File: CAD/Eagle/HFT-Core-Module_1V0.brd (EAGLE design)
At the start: 96.5 x 96.5 mm, 341 parts, among them Q0521 ABS07-32.768KHZ, Q0911 ABM3B-16MHZ-10-R50-1-U, T0801 MMBT2222, T0802 MMBT2222, T0803 MMBT2222, U0111 STM32L4Z_144PIN_SMPS, U0431 PAM2305AAB120, U0601 LM4120IM5-3.0, U0611 MAX5217, U0631 CFPT-141-20MHZ, U0641 OPA354, U0701 Si5338, U0801 NHD-C0220BIZ_2X20CHARS, U0901 AX5243, U1001 AX5243, U1101 MCP3911A0-E-SS, U1111 MAX5136AGTG+, U1121 OPA354, U1131 OPA354, U1141 OPA354, U1601 SOLARPANEL_3V3_5MA1_25MM_X_20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, U1602 SPV1040T, U1701 TS5A23166, U1801 PAM2305AAB330, U1901 TS5A23166, U2001 TS5A23166, U2101 TS5A23166, X0861 TTE_EN11-HSM, X1401 SMA_SMT_AMPHENOL-901-143, X1411 SMA_SMT_AMPHENOL-901-143, X1501 CUI SJ1-3535NS, X1511 CUI SJ1-3535NS, X511 2X20/90_1MM27_HARWIN_M50-3202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, X512 2X20/90_1MM27_HARWIN_M50-3202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, X521 2X20/90_1MM27_HARWIN_M50-3202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, X522 2X20/90_1MM27_HARWIN_M50-3202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, X531 2X20/90_1MM27_HARWIN_M50-3202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, X532 2X20/90_1MM27_HARWIN_M50-3202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

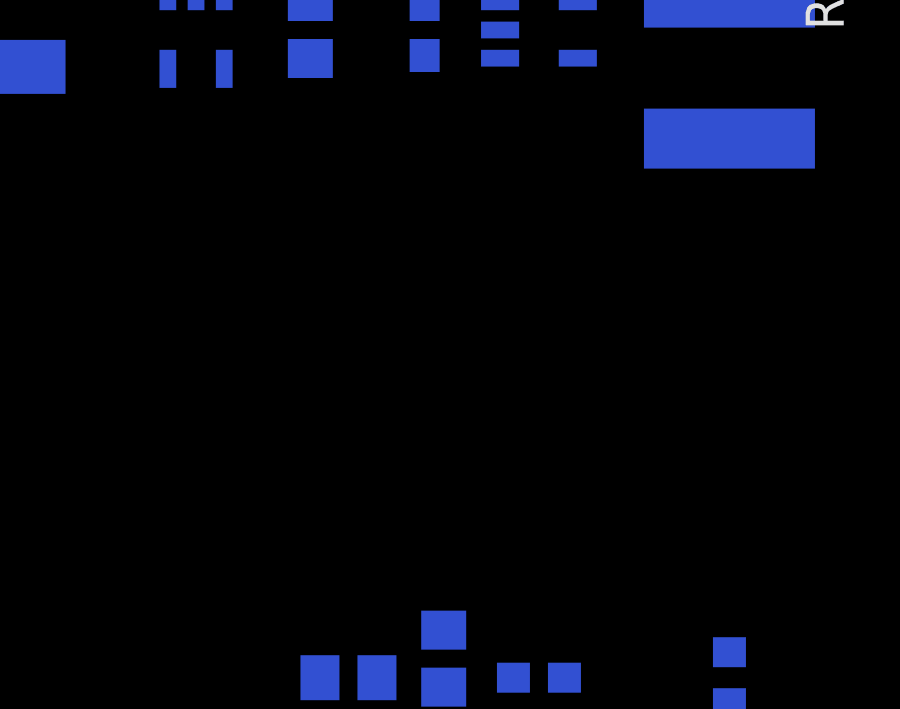
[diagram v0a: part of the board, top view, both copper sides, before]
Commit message: HW_1V0 - MPU-9250 added and placed
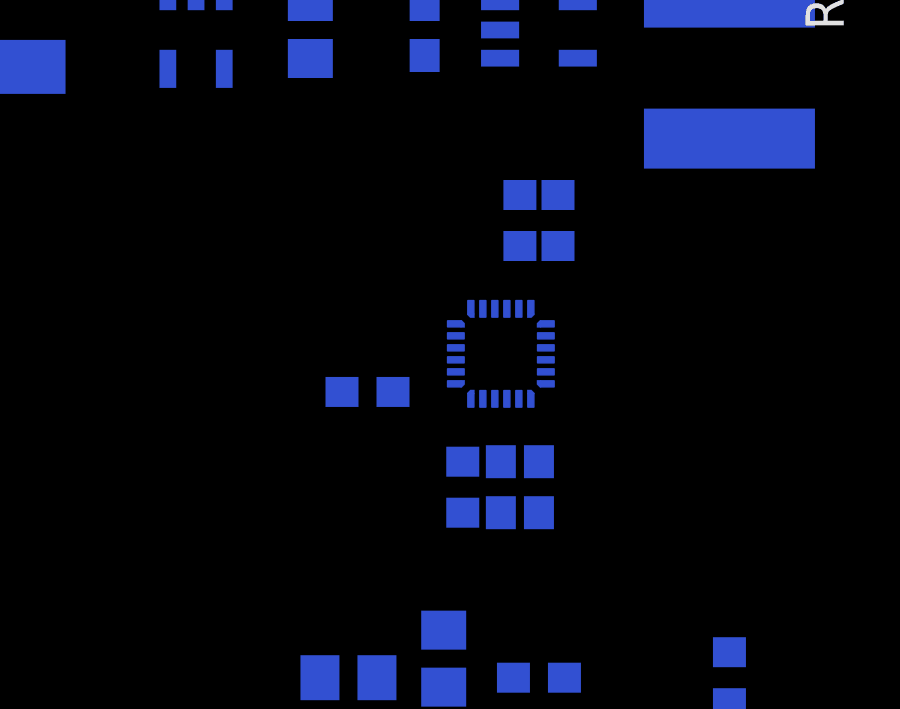
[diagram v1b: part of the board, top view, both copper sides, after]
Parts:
- added C2301, C2303: 100nF, rcl:C0603
- added C2302: 10nF, rcl:C0603
- added R2301: 68R, rcl:R0603
- added R2311, R2312: 3.9kR, rcl:R0603
- added U2301: MPU-9250, df4iah_sensors:QFN24-3X3
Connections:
- new net I2C2_INT: R2301.2
- new net MPU_INT: R2301.1, U2301.12
- new net MPU_REGOUT: C2303.1, U2301.10
- net +3V3: now also C2301.1, C2302.1, R2311.2, R2312.2, U2301.1, U2301.13, U2301.22, U2301.8
- net GND: now also C2301.2, C2302.2, C2303.2, U2301.11, U2301.18, U2301.20, U2301.9
- net MCU_I2C4_SCL: now also R2312.1, U2301.23
- net MCU_I2C4_SDA: now also R2311.1, U2301.24
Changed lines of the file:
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@@
 <element name="R0804" library="rcl" package="R0603" value="2.2kR" x="59.055" y="47.625" rot="R90"/>
 <element name="R0801" library="rcl" package="R0603" value="1.8kR" x="80.645" y="65.405" rot="MR0"/>
+<element name="U2301" library="df4iah_sensors" package="QFN24-3X3" value="MPU-9250" x="48.26" y="23.495" rot="MR0"/>
+<element name="C2301" library="rcl" package="C0603" value="100nF" x="49.53" y="19.05" rot="MR270"/>
+<element name="C2303" library="rcl" package="C0603" value="100nF" x="48.26" y="19.05" rot="MR270"/>
+<element name="R2301" library="rcl" package="R0603" value="68R" x="46.99" y="19.05" rot="MR270"/>
+<element name="C2302" library="rcl" package="C0603" value="10nF" x="43.815" y="22.225" rot="MR0"/>
+<element name="R2311" library="rcl" package="R0603" value="3.9kR" x="50.165" y="27.94" rot="MR90"/>
+<element name="R2312" library="rcl" package="R0603" value="3.9kR" x="48.895" y="27.94" rot="MR90"/>
 </elements>
 <signals>
@@
 <contactref element="R0802" pad="1"/>
 <contactref element="R0805" pad="1"/>
+<contactref element="U2301" pad="9"/>
+<contactref element="C2301" pad="2"/>
+<contactref element="U2301" pad="20"/>
+<contactref element="U2301" pad="18"/>
+<contactref element="U2301" pad="11"/>
+<contactref element="C2303" pad="2"/>
+<contactref element="C2302" pad="2"/>
 <wire x1="93.7025" y1="87.6" x2="91.44" y2="91.44" width="0" layer="19" extent="1-1"/>
 <wire x1="93.56" y1="85.725" x2="93.7025" y2="87.6" width="0" layer="19" extent="16-16"/>
@@
 <wire x1="63.285" y1="11.43" x2="63.285" y2="10.16" width="0" layer="19" extent="16-16"/>
 <wire x1="46.355" y1="14.285" x2="50.38" y2="12.7" width="0" layer="19" extent="16-16"/>
+<wire x1="48.26" y1="18.2" x2="46.355" y2="14.285" width="0" layer="19" extent="16-16"/>
+<wire x1="49.53" y1="18.2" x2="48.26" y2="18.2" width="0" layer="19" extent="16-16"/>
+<wire x1="48.46" y1="21.995" x2="48.26" y2="18.2" width="0" layer="19" extent="16-16"/>
+<wire x1="47.66" y1="21.995" x2="48.46" y2="21.995" width="0" layer="19" extent="16-16"/>
+<wire x1="46.7075" y1="24.495" x2="47.66" y2="21.995" width="0" layer="19" extent="16-16"/>
+<wire x1="47.66" y1="24.995" x2="46.7075" y2="24.495" width="0" layer="19" extent="16-16"/>
+<wire x1="42.965" y1="22.225" x2="46.7075" y2="24.495" width="0" layer="19" extent="16-16"/>
 <wire x1="62.23" y1="2.54" x2="62.23" y2="7.62" width="0" layer="19" extent="1-1"/>
 <wire x1="58.42" y1="2.54" x2="62.23" y2="2.54" width="0" layer="19" extent="1-1"/>
@@
 <contactref element="U0111" pad="106"/>
 <contactref element="U0801" pad="12"/>
+<contactref element="U2301" pad="8"/>
+<contactref element="U2301" pad="1"/>
+<contactref element="U2301" pad="13"/>
+<contactref element="C2301" pad="1"/>
+<contactref element="U2301" pad="22"/>
+<contactref element="C2302" pad="1"/>
+<contactref element="R2311" pad="2"/>
+<contactref element="R2312" pad="2"/>
 <wire x1="73.66" y1="88.9" x2="85.09" y2="90.17" width="0" layer="19" extent="1-1"/>
 <wire x1="73.66" y1="93.98" x2="73.66" y2="88.9" width="0" layer="19" extent="1-1"/>
@@
 <wire x1="48.2346" y1="35.2298" x2="45.72" y2="35.14" width="0" layer="19" extent="16-16"/>
 <wire x1="48.2346" y1="33.3502" x2="48.2346" y2="35.2298" width="0" layer="19" extent="16-16"/>
+<wire x1="48.895" y1="28.79" x2="48.2346" y2="33.3502" width="0" layer="19" extent="16-16"/>
+<wire x1="50.165" y1="28.79" x2="48.895" y2="28.79" width="0" layer="19" extent="16-16"/>
+<wire x1="48.46" y1="24.995" x2="48.895" y2="28.79" width="0" layer="19" extent="16-16"/>
+<wire x1="49.8125" y1="24.495" x2="48.46" y2="24.995" width="0" layer="19" extent="16-16"/>
+<wire x1="48.86" y1="21.995" x2="49.8125" y2="24.495" width="0" layer="19" extent="16-16"/>
+<wire x1="49.53" y1="19.9" x2="48.86" y2="21.995" width="0" layer="19" extent="16-16"/>
+<wire x1="46.7075" y1="22.495" x2="48.86" y2="21.995" width="0" layer="19" extent="16-16"/>
+<wire x1="44.665" y1="22.225" x2="46.7075" y2="22.495" width="0" layer="19" extent="16-16"/>
+<wire x1="48.68" y1="12.7" x2="49.53" y2="19.9" width="0" layer="19" extent="16-16"/>
+<wire x1="48.276" y1="10.13" x2="48.68" y2="12.7" width="0" layer="19" extent="16-16"/>
 <wire x1="59.335" y1="37.985" x2="48.2346" y2="35.2298" width="0" layer="19" extent="16-16"/>
 <wire x1="60.96" y1="37.885" x2="59.335" y2="37.985" width="0" layer="19" extent="16-16"/>
@@
 <wire x1="73.66" y1="7.62" x2="68.85" y2="16.455" width="0" layer="19" extent="16-16"/>
 <wire x1="73.66" y1="2.54" x2="73.66" y2="7.62" width="0" layer="19" extent="1-1"/>
-<wire x1="48.68" y1="12.7" x2="68.16" y2="17.145" width="0" layer="19" extent="16-16"/>
-<wire x1="48.276" y1="10.13" x2="48.68" y2="12.7" width="0" layer="19" extent="16-16"/>
 <wire x1="22.86" y1="7.62" x2="48.276" y2="10.13" width="0" layer="19" extent="1-1"/>
 <wire x1="22.86" y1="2.54" x2="22.86" y2="7.62" width="0" layer="19" extent="1-1"/>
@@
 <contactref element="U0701" pad="12"/>
 <contactref element="R0231" pad="2"/>
+<contactref element="U2301" pad="23"/>
+<contactref element="R2312" pad="1"/>
 <wire x1="41.03" y1="83.495" x2="70.53" y2="84.435" width="0" layer="19" extent="1-1"/>
 <wire x1="66.04" y1="46.775" x2="70.53" y2="84.435" width="0" layer="19" extent="1-1"/>
-<wire x1="54.276" y1="10.13" x2="66.04" y2="46.775" width="0" layer="19" extent="1-1"/>
+<wire x1="48.895" y1="27.09" x2="66.04" y2="46.775" width="0" layer="19" extent="1-16"/>
+<wire x1="48.86" y1="24.995" x2="48.895" y2="27.09" width="0" layer="19" extent="16-16"/>
+<wire x1="54.276" y1="10.13" x2="48.86" y2="24.995" width="0" layer="19" extent="16-16"/>
 </signal>
 <signal name="MCU_I2C4_SDA">
@@
 <contactref element="U0701" pad="19"/>
 <contactref element="R0232" pad="2"/>
+<contactref element="U2301" pad="24"/>
+<contactref element="R2311" pad="1"/>
 <wire x1="41.03" y1="82.845" x2="66.63" y2="84.435" width="0" layer="19" extent="1-1"/>
 <wire x1="81.495" y1="58.42" x2="66.63" y2="84.435" width="0" layer="19" extent="1-1"/>
-<wire x1="52.276" y1="10.13" x2="81.495" y2="58.42" width="0" layer="19" extent="1-1"/>
+<wire x1="50.165" y1="27.09" x2="81.495" y2="58.42" width="0" layer="19" extent="1-16"/>
+<wire x1="49.26" y1="25.0475" x2="50.165" y2="27.09" width="0" layer="19" extent="16-16"/>
+<wire x1="52.276" y1="10.13" x2="49.26" y2="25.0475" width="0" layer="19" extent="16-16"/>
 </signal>
 <signal name="MCU_I2C2_SCL">
@@
 <wire x1="10.726" y1="28.18" x2="16.045" y2="22.86" width="0" layer="19" extent="16-16"/>
 </signal>
+<signal name="MPU_REGOUT">
+<contactref element="U2301" pad="10"/>
+<contactref element="C2303" pad="1"/>
+<wire x1="48.26" y1="19.9" x2="48.06" y2="21.995" width="0" layer="19" extent="16-16"/>
+</signal>
+<signal name="I2C2_INT">
+<contactref element="R2301" pad="2"/>
+</signal>
+<signal name="MPU_INT">
+<contactref element="U2301" pad="12"/>
+<contactref element="R2301" pad="1"/>
+<wire x1="46.99" y1="19.9" x2="47.26" y2="21.9425" width="0" layer="19" extent="16-16"/>
+</signal>
 </signals>

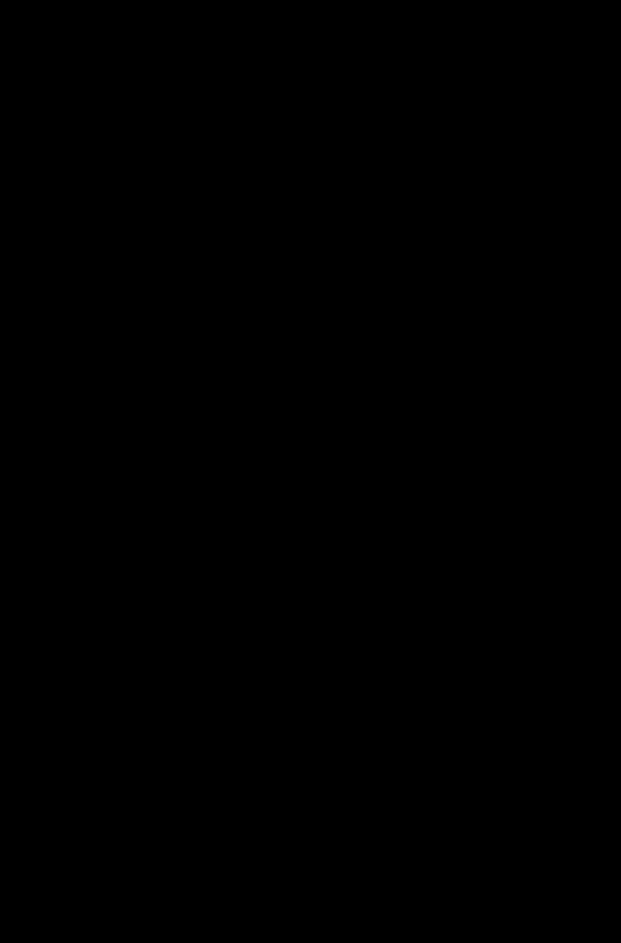
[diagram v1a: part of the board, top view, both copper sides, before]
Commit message: HW_1V0 - more I2C sensors added
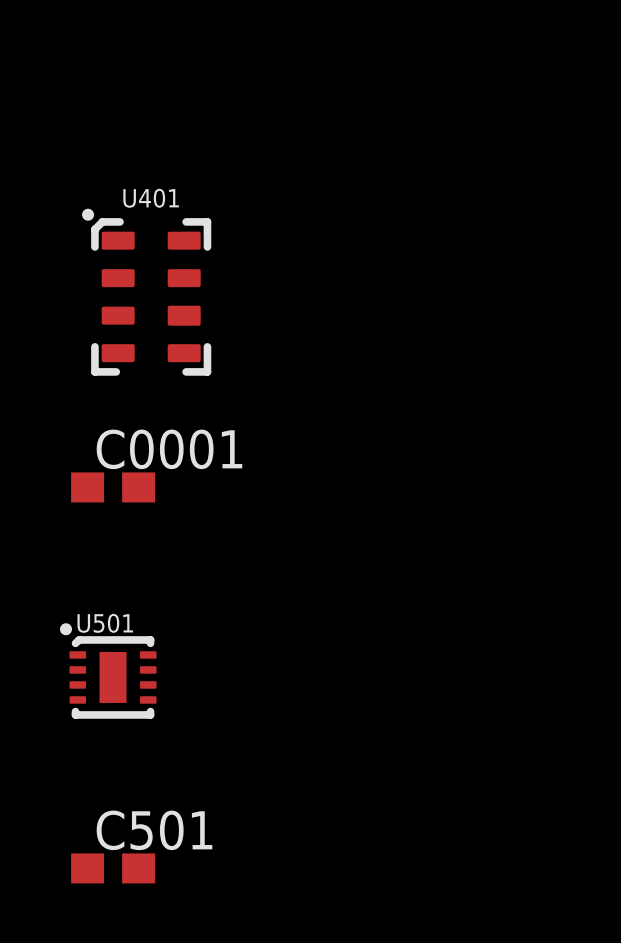
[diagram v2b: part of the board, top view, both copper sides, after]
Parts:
- added C0001, C501: 100nF, rcl:C0603
- added U401: MS5607-02BA03, df4iah_sensors:MS5607-02BA
- added U501: SHT31-DIS, df4iah_sensors:DFN8/SHT
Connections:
- net +3V3: now also C0001.1, C501.1, U401.1, U401.2, U401.4, U501.5, U501.6
- net GND: now also C0001.2, C501.2, U401.3, U501.2, U501.7, U501.8, U501.9
- net MCU_I2C4_SCL: now also U401.8, U501.4
- net MCU_I2C4_SDA: now also U401.7, U501.1
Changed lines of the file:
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@@
 <element name="R2311" library="rcl" package="R0603" value="3.9kR" x="50.165" y="27.94" rot="MR90"/>
 <element name="R2312" library="rcl" package="R0603" value="3.9kR" x="48.895" y="27.94" rot="MR90"/>
+<element name="C0001" library="rcl" package="C0603" value="100nF" x="-25.4" y="-39.37"/>
+<element name="U401" library="df4iah_sensors" package="MS5607-02BA" value="MS5607-02BA03" x="-24.13" y="-33.02"/>
+<element name="U501" library="df4iah_sensors" package="DFN8/SHT" value="SHT31-DIS" x="-25.4" y="-45.72"/>
+<element name="C501" library="rcl" package="C0603" value="100nF" x="-25.4" y="-52.07"/>
 </elements>
 <signals>
@@
 <contactref element="C2303" pad="2"/>
 <contactref element="C2302" pad="2"/>
+<contactref element="C0001" pad="2"/>
+<contactref element="U401" pad="3"/>
+<contactref element="C501" pad="2"/>
+<contactref element="U501" pad="9"/>
+<contactref element="U501" pad="8"/>
+<contactref element="U501" pad="2"/>
+<contactref element="U501" pad="7"/>
 <wire x1="93.7025" y1="87.6" x2="91.44" y2="91.44" width="0" layer="19" extent="1-1"/>
 <wire x1="93.56" y1="85.725" x2="93.7025" y2="87.6" width="0" layer="19" extent="16-16"/>
@@
 <wire x1="5.08" y1="91.44" x2="21.59" y2="93.98" width="0" layer="19" extent="1-1"/>
 <wire x1="5.08" y1="5.08" x2="21.59" y2="7.62" width="0" layer="19" extent="1-1"/>
+<wire x1="-25.23" y1="-33.645" x2="5.08" y2="5.08" width="0" layer="19" extent="1-1"/>
+<wire x1="-24.55" y1="-39.37" x2="-25.23" y2="-33.645" width="0" layer="19" extent="1-1"/>
+<wire x1="-24.227409375" y1="-44.95478125" x2="-24.55" y2="-39.37" width="0" layer="19" extent="1-1"/>
+<wire x1="-24.227409375" y1="-45.45478125" x2="-24.227409375" y2="-44.95478125" width="0" layer="19" extent="1-1"/>
+<wire x1="-25.402409375" y1="-45.70478125" x2="-24.227409375" y2="-45.45478125" width="0" layer="19" extent="1-1"/>
+<wire x1="-26.577409375" y1="-45.45478125" x2="-25.402409375" y2="-45.70478125" width="0" layer="19" extent="1-1"/>
+<wire x1="-24.55" y1="-52.07" x2="-25.402409375" y2="-45.70478125" width="0" layer="19" extent="1-1"/>
 </signal>
 <signal name="MCU_VSSA">
@@
 <contactref element="U2301" pad="13"/>
 <contactref element="C2301" pad="1"/>
-<contactref element="U2301" pad="22"/>
 <contactref element="C2302" pad="1"/>
 <contactref element="R2311" pad="2"/>
 <contactref element="R2312" pad="2"/>
+<contactref element="C0001" pad="1"/>
+<contactref element="U401" pad="1"/>
+<contactref element="U401" pad="2"/>
+<contactref element="U401" pad="4"/>
+<contactref element="U2301" pad="22"/>
+<contactref element="C501" pad="1"/>
+<contactref element="U501" pad="5"/>
+<contactref element="U501" pad="6"/>
 <wire x1="73.66" y1="88.9" x2="85.09" y2="90.17" width="0" layer="19" extent="1-1"/>
 <wire x1="73.66" y1="93.98" x2="73.66" y2="88.9" width="0" layer="19" extent="1-1"/>
@@
 <wire x1="22.86" y1="88.9" x2="7.62" y2="73.66" width="0" layer="19" extent="1-1"/>
 <wire x1="22.86" y1="93.98" x2="22.86" y2="88.9" width="0" layer="19" extent="1-1"/>
+<wire x1="-25.23" y1="-31.145" x2="22.86" y2="2.54" width="0" layer="19" extent="1-1"/>
+<wire x1="-25.23" y1="-32.395" x2="-25.23" y2="-31.145" width="0" layer="19" extent="1-1"/>
+<wire x1="-25.23" y1="-34.895" x2="-25.23" y2="-32.395" width="0" layer="19" extent="1-1"/>
+<wire x1="-26.25" y1="-39.37" x2="-25.23" y2="-34.895" width="0" layer="19" extent="1-1"/>
+<wire x1="-24.227409375" y1="-45.95478125" x2="-26.25" y2="-39.37" width="0" layer="19" extent="1-1"/>
+<wire x1="-24.227409375" y1="-46.45478125" x2="-24.227409375" y2="-45.95478125" width="0" layer="19" extent="1-1"/>
+<wire x1="-26.25" y1="-52.07" x2="-24.227409375" y2="-46.45478125" width="0" layer="19" extent="1-1"/>
 </signal>
 <signal name="XO_LP">
@@
 <contactref element="U2301" pad="23"/>
 <contactref element="R2312" pad="1"/>
+<contactref element="U401" pad="8"/>
+<contactref element="U501" pad="4"/>
 <wire x1="41.03" y1="83.495" x2="70.53" y2="84.435" width="0" layer="19" extent="1-1"/>
 <wire x1="66.04" y1="46.775" x2="70.53" y2="84.435" width="0" layer="19" extent="1-1"/>
@@
 <wire x1="48.86" y1="24.995" x2="48.895" y2="27.09" width="0" layer="19" extent="16-16"/>
 <wire x1="54.276" y1="10.13" x2="48.86" y2="24.995" width="0" layer="19" extent="16-16"/>
+<wire x1="-23.03" y1="-31.145" x2="54.276" y2="10.13" width="0" layer="19" extent="1-1"/>
+<wire x1="-26.577409375" y1="-46.45478125" x2="-23.03" y2="-31.145" width="0" layer="19" extent="1-1"/>
 </signal>
 <signal name="MCU_I2C4_SDA">
@@
 <contactref element="U2301" pad="24"/>
 <contactref element="R2311" pad="1"/>
+<contactref element="U401" pad="7"/>
+<contactref element="U501" pad="1"/>
 <wire x1="41.03" y1="82.845" x2="66.63" y2="84.435" width="0" layer="19" extent="1-1"/>
 <wire x1="81.495" y1="58.42" x2="66.63" y2="84.435" width="0" layer="19" extent="1-1"/>
@@
 <wire x1="49.26" y1="25.0475" x2="50.165" y2="27.09" width="0" layer="19" extent="16-16"/>
 <wire x1="52.276" y1="10.13" x2="49.26" y2="25.0475" width="0" layer="19" extent="16-16"/>
+<wire x1="-23.03" y1="-32.395" x2="52.276" y2="10.13" width="0" layer="19" extent="1-1"/>
+<wire x1="-26.577409375" y1="-44.95478125" x2="-23.03" y2="-32.395" width="0" layer="19" extent="1-1"/>
 </signal>
 <signal name="MCU_I2C2_SCL">
